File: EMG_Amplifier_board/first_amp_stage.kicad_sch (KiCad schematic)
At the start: 9 parts, among them U2 INA333xxDGK, U3 LPV821DBVR

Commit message: add footprints
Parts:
- C3, C4: footprint (none) -> Capacitor_SMD:C_0805_2012Metric
- R10: renamed from R7; footprint (none) -> Resistor_SMD:R_0805_2012Metric
- R11: renamed from R6; footprint (none) -> Resistor_SMD:R_0805_2012Metric
- R12: renamed from R5; value 150kOhm -> 150kR; footprint (none) -> Resistor_SMD:R_0805_2012Metric
- R13: renamed from R3; footprint (none) -> Resistor_SMD:R_0805_2012Metric
- R14: renamed from R4; footprint (none) -> Resistor_SMD:R_0805_2012Metric
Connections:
- net VDD/2 renamed V_DD/2
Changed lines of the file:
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@@
+	(wire
+		(pts
+			(xy 162.56 105.41) (xy 165.1 105.41)
+		)
+		(stroke
+			(width 0)
+			(type default)
+		)
+	)
 	(wire
 		(pts
@@
 	(wire
 		(pts
-			(xy 165.1 96.52) (xy 165.1 102.87)
+			(xy 165.1 105.41) (xy 165.1 124.46)
 		)
 		(stroke
@@
 		)
 	)
+	(wire
+		(pts
+			(xy 165.1 96.52) (xy 165.1 102.87)
+		)
+		(stroke
+			(width 0)
+			(type default)
+		)
+	)
+	(hierarchical_label "V_DD{slash}2"
+		(shape input)
+		(at 165.1 124.46 270)
+		(fields_autoplaced yes)
+		(effects
+			(font
+				(size 1.27 1.27)
+			)
+			(justify right)
+		)
+	)
 	(hierarchical_label "+V_DD"
 		(shape input)
@@
 			)
 			(justify left)
+		)
+	)
+	(hierarchical_label "GND"
+		(shape input)
+		(at 185.42 118.11 270)
+		(fields_autoplaced yes)
+		(effects
+			(font
+				(size 1.27 1.27)
+			)
+			(justify right)
 		)
 	)
@@
 		(on_board yes)
 		(dnp no)
-		(property "Reference" "R4"
+		(property "Reference" "R14"
 			(at 97.79 84.328 90)
 			(effects
@@
 			)
 		)
-		(property "Footprint" ""
+		(property "Footprint" "Resistor_SMD:R_0805_2012Metric"
 			(at 97.79 83.058 90)
 			(effects
@@
 			(project "EMG_amplifier"
 				(path "/26861adc-1ddf-4c37-9f8b-8db1c0839771/303f9ad4-7b95-498e-980d-614d18323dab"
-					(reference "R4")
-					(unit 1)
-				)
-			)
-		)
-	)
-	(symbol
-		(lib_id "power:VCC")
-		(at 162.56 105.41 270)
-		(unit 1)
-		(exclude_from_sim no)
-		(in_bom yes)
-		(on_board yes)
-		(dnp no)
-		(property "Reference" "#PWR08"
-			(at 158.75 105.41 0)
-			(effects
-				(font
-					(size 1.27 1.27)
-				)
-				(hide yes)
-			)
-		)
-		(property "Value" "VDD/2"
-			(at 166.37 105.4099 90)
-			(effects
-				(font
-					(size 1.27 1.27)
-				)
-				(justify left)
-			)
-		)
-		(property "Footprint" ""
-			(at 162.56 105.41 0)
-			(effects
-				(font
-					(size 1.27 1.27)
-				)
-				(hide yes)
-			)
-		)
-		(property "Datasheet" ""
-			(at 162.56 105.41 0)
-			(effects
-				(font
-					(size 1.27 1.27)
-				)
-				(hide yes)
-			)
-		)
-		(property "Description" "Power symbol creates a global label with name \"VCC\""
-			(at 162.56 105.41 0)
-			(effects
-				(font
-					(size 1.27 1.27)
-				)
-				(hide yes)
-			)
-		)
-		(pin "1"
-		)
-		(instances
-			(project "EMG_amplifier"
-				(path "/26861adc-1ddf-4c37-9f8b-8db1c0839771/303f9ad4-7b95-498e-980d-614d18323dab"
-					(reference "#PWR08")
+					(reference "R14")
 					(unit 1)
 				)
@@
 		(dnp no)
 		(fields_autoplaced yes)
-		(property "Reference" "R7"
+		(property "Reference" "R10"
 			(at 200.66 91.4399 0)
 			(effects
@@
 			)
 		)
-		(property "Footprint" ""
+		(property "Footprint" "Resistor_SMD:R_0805_2012Metric"
 			(at 199.898 92.71 90)
 			(effects
@@
 			(project "EMG_amplifier"
 				(path "/26861adc-1ddf-4c37-9f8b-8db1c0839771/303f9ad4-7b95-498e-980d-614d18323dab"
-					(reference "R7")
+					(reference "R10")
 					(unit 1)
 				)
@@
 			)
 		)
-		(property "Footprint" ""
+		(property "Footprint" "Capacitor_SMD:C_0805_2012Metric"
 			(at 186.3852 118.11 0)
 			(effects
@@
 		(on_board yes)
 		(dnp no)
-		(property "Reference" "R6"
+		(property "Reference" "R11"
 			(at 187.96 91.4399 0)
 			(effects
@@
 			)
 		)
-		(property "Footprint" ""
+		(property "Footprint" "Resistor_SMD:R_0805_2012Metric"
 			(at 187.198 92.71 90)
 			(effects
@@
 			(project "EMG_amplifier"
 				(path "/26861adc-1ddf-4c37-9f8b-8db1c0839771/303f9ad4-7b95-498e-980d-614d18323dab"
-					(reference "R6")
+					(reference "R11")
 					(unit 1)
 				)
@@
 			)
 		)
-		(property "Footprint" ""
+		(property "Footprint" "Capacitor_SMD:C_0805_2012Metric"
 			(at 166.0652 96.52 0)
 			(effects
@@
 				(path "/26861adc-1ddf-4c37-9f8b-8db1c0839771/303f9ad4-7b95-498e-980d-614d18323dab"
 					(reference "C3")
-					(unit 1)
-				)
-			)
-		)
-	)
-	(symbol
-		(lib_id "power:GND")
-		(at 185.42 118.11 0)
-		(unit 1)
-		(exclude_from_sim no)
-		(in_bom yes)
-		(on_board yes)
-		(dnp no)
-		(fields_autoplaced yes)
-		(property "Reference" "#PWR09"
-			(at 185.42 124.46 0)
-			(effects
-				(font
-					(size 1.27 1.27)
-				)
-				(hide yes)
-			)
-		)
-		(property "Value" "GND"
-			(at 185.42 123.19 0)
-			(effects
-				(font
-					(size 1.27 1.27)
-				)
-			)
-		)
-		(property "Footprint" ""
-			(at 185.42 118.11 0)
-			(effects
-				(font
-					(size 1.27 1.27)
-				)
-				(hide yes)
-			)
-		)
-		(property "Datasheet" ""
-			(at 185.42 118.11 0)
-			(effects
-				(font
-					(size 1.27 1.27)
-				)
-				(hide yes)
-			)
-		)
-		(property "Description" "Power symbol creates a global label with name \"GND\" , ground"
-			(at 185.42 118.11 0)
-			(effects
-				(font
-					(size 1.27 1.27)
-				)
-				(hide yes)
-			)
-		)
-		(pin "1"
-		)
-		(instances
-			(project "EMG_amplifier"
-				(path "/26861adc-1ddf-4c37-9f8b-8db1c0839771/303f9ad4-7b95-498e-980d-614d18323dab"
-					(reference "#PWR09")
 					(unit 1)
 				)
@@
 		(on_board yes)
 		(dnp no)
-		(property "Reference" "R5"
+		(property "Reference" "R12"
 			(at 175.26 98.044 90)
 			(effects
@@
 			)
 		)
-		(property "Value" "150kOhm"
+		(property "Value" "150kR"
 			(at 175.26 100.584 90)
 			(effects
@@
 			)
 		)
-		(property "Footprint" ""
+		(property "Footprint" "Resistor_SMD:R_0805_2012Metric"
 			(at 175.26 104.648 90)
 			(effects
@@
 			(project "EMG_amplifier"
 				(path "/26861adc-1ddf-4c37-9f8b-8db1c0839771/303f9ad4-7b95-498e-980d-614d18323dab"
-					(reference "R5")
+					(reference "R12")
 					(unit 1)
 				)
@@
 		(on_board yes)
 		(dnp no)
-		(property "Reference" "R3"
+		(property "Reference" "R13"
 			(at 98.044 71.374 90)
 			(effects
@@
 			)
 		)
-		(property "Footprint" ""
+		(property "Footprint" "Resistor_SMD:R_0805_2012Metric"
 			(at 97.79 77.978 90)
 			(effects
@@
 			(project "EMG_amplifier"
 				(path "/26861adc-1ddf-4c37-9f8b-8db1c0839771/303f9ad4-7b95-498e-980d-614d18323dab"
-					(reference "R3")
+					(reference "R13")
 					(unit 1)
 				)

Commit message: acomponents choice
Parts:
- C3: footprint Capacitor_SMD:C_0805_2012Metric -> Capacitor_SMD:C_0603_1608Metric
- C4: footprint Capacitor_SMD:C_0805_2012Metric -> Capacitor_SMD:C_0201_0603Metric
- R10, R11, R12: footprint Resistor_SMD:R_0805_2012Metric -> Resistor_SMD:R_01005_0402Metric
- R13, R14: footprint Resistor_SMD:R_0805_2012Metric -> Resistor_SMD:R_0201_0603Metric
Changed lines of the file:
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@@
 			)
 		)
-		(property "Footprint" "Resistor_SMD:R_0805_2012Metric"
+		(property "Footprint" "Resistor_SMD:R_0201_0603Metric"
 			(at 97.79 83.058 90)
 			(effects
@@
 			)
 		)
-		(property "Footprint" "Resistor_SMD:R_0805_2012Metric"
+		(property "Footprint" "Resistor_SMD:R_01005_0402Metric"
 			(at 199.898 92.71 90)
 			(effects
@@
 			)
 		)
-		(property "Footprint" "Capacitor_SMD:C_0805_2012Metric"
+		(property "Footprint" "Capacitor_SMD:C_0201_0603Metric"
 			(at 186.3852 118.11 0)
 			(effects
@@
 			)
 		)
-		(property "Footprint" "Resistor_SMD:R_0805_2012Metric"
+		(property "Footprint" "Resistor_SMD:R_01005_0402Metric"
 			(at 187.198 92.71 90)
 			(effects
@@
 			)
 		)
-		(property "Footprint" "Capacitor_SMD:C_0805_2012Metric"
+		(property "Footprint" "Capacitor_SMD:C_0603_1608Metric"
 			(at 166.0652 96.52 0)
 			(effects
@@
 			)
 		)
-		(property "Footprint" "Resistor_SMD:R_0805_2012Metric"
+		(property "Footprint" "Resistor_SMD:R_01005_0402Metric"
 			(at 175.26 104.648 90)
 			(effects
@@
 			)
 		)
-		(property "Footprint" "Resistor_SMD:R_0805_2012Metric"
+		(property "Footprint" "Resistor_SMD:R_0201_0603Metric"
 			(at 97.79 77.978 90)
 			(effects

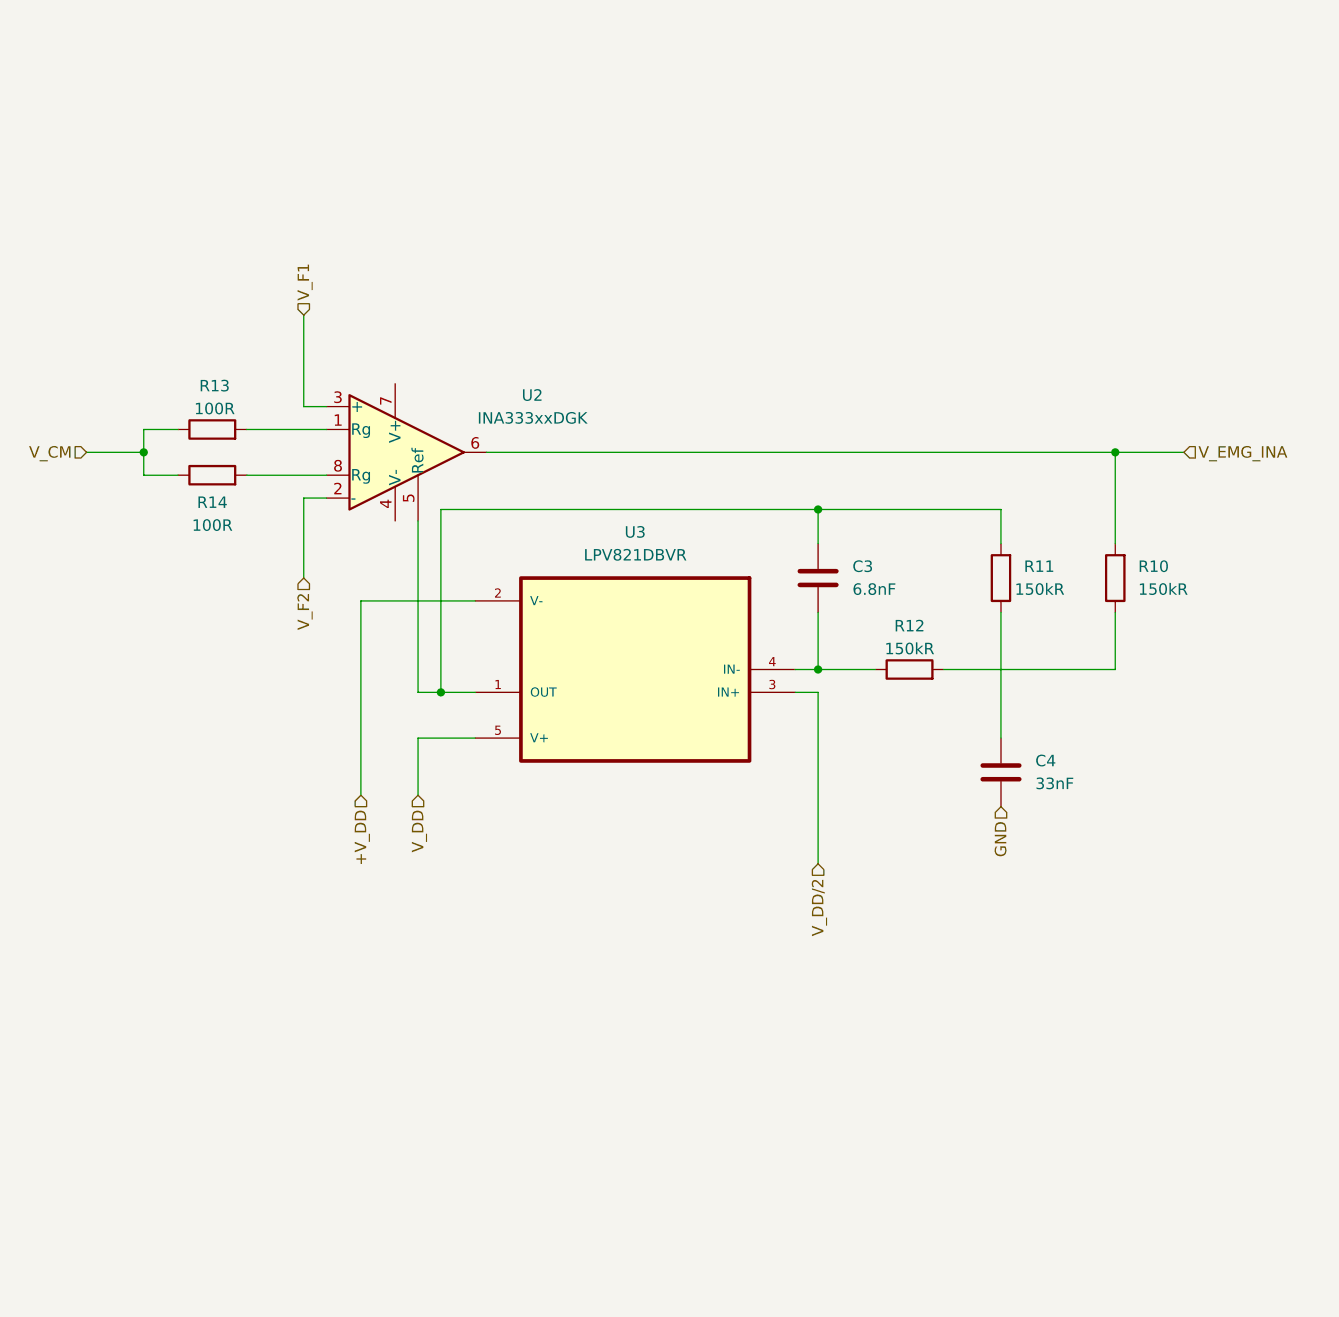
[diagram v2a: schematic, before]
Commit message: update the schematic with shared grounds and pin connectors
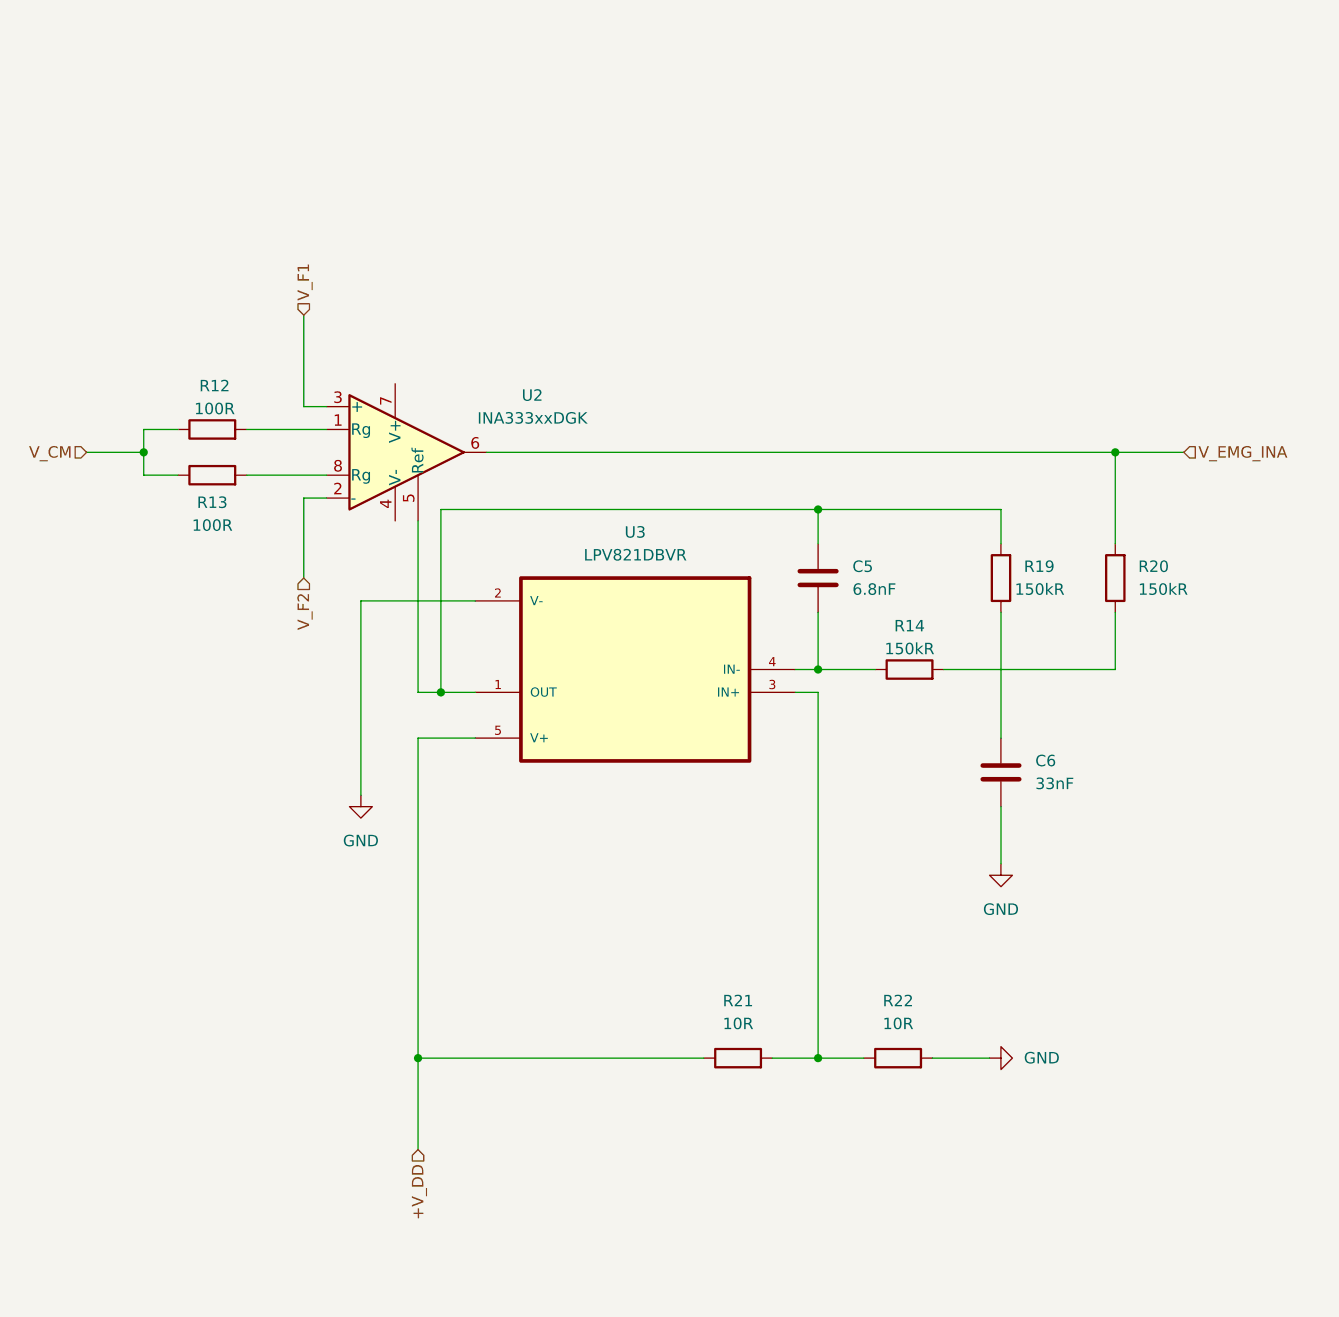
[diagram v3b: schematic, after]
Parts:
- added R21, R22: 10R, Resistor_SMD:R_0402_1005Metric, symbol Device:R
- renumbered C3 to C5, C4 to C6, R13 to R12, R14 to R13, R12 to R14, R11 to R19, R10 to R20
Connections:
- net V_DD is gone; now on net +V_DD: U3.5 (V+)
- net +V_DD: now also R21.1; no longer U3.2 (V-)
- net GND: now also U3.2 (V-), R22.2
- net V_DD/2: no longer names the net of U3.3 (IN+)
- net V_DD/2: now also R21.2, R22.1

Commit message: pcb design v1
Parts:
- added C10, C9: 0.1uF, Capacitor_SMD:C_0805_2012Metric, symbol Device:C_Small
- C6: footprint Capacitor_SMD:C_0201_0603Metric -> Capacitor_SMD:C_0805_2012Metric
- R12, R13: footprint Resistor_SMD:R_0201_0603Metric -> Resistor_SMD:R_0402_1005Metric
- R14, R19, R20: footprint Resistor_SMD:R_01005_0402Metric -> Resistor_SMD:R_0402_1005Metric
- R21, R22: value 10R -> 10k
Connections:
- net +V_DD: now also U2.7 (V+), C10.1, C9.1
- net GND: now also U2.4 (V-), C10.2, C9.2
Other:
- moved on the sheet: C6
